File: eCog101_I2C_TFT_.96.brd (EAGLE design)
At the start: 48 x 28 mm, 3 parts

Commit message: Added parts to attributes for BOM
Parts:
- JP1: value (none) -> .96 I2C OLED LCD
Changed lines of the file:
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@@
 </autorouter>
 <elements>
-<element name="ECOG" library="eCogs" package="ECOG_BUSES_SMD" value="ECOG_BUSES_ROWECOG_BUSES_SMD" x="0" y="0" smashed="yes"/>
-<element name="JP1" library="pinhead" package="1X04" value="" x="24" y="25.4" smashed="yes">
+<element name="ECOG" library="eCogs" package="ECOG_BUSES_SMD" value="ECOG_BUSES_ROWECOG_BUSES_SMD" x="0" y="0" smashed="yes">
+<attribute name="DIGIKEY" value="S1013EC-10-ND" x="0" y="0" size="1.778" layer="27" display="off"/>
+</element>
+<element name="JP1" library="pinhead" package="1X04" value=".96 I2C OLED LCD" x="24" y="25.4" smashed="yes">
 <attribute name="VALUE" x="18.92" y="22.225" size="1.27" layer="27"/>
+<attribute name="DEALEXTREME" value="419232" x="24" y="25.4" size="1.778" layer="27" display="off"/>
 </element>
 <element name="U$1" library="GadgetFactory" package="GADGETBOX_TEXT" value="" x="24.13" y="13.97"/>

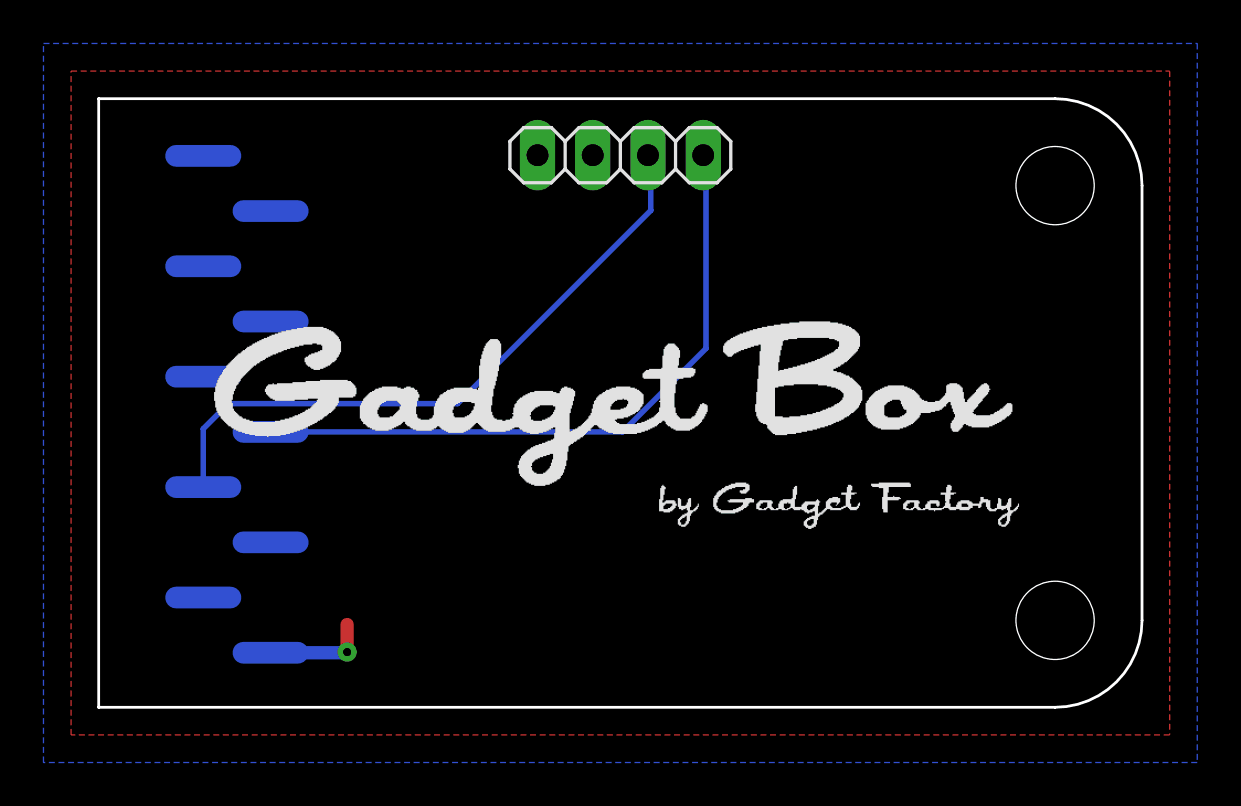
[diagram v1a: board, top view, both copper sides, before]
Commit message: Added Box text to silkscreen
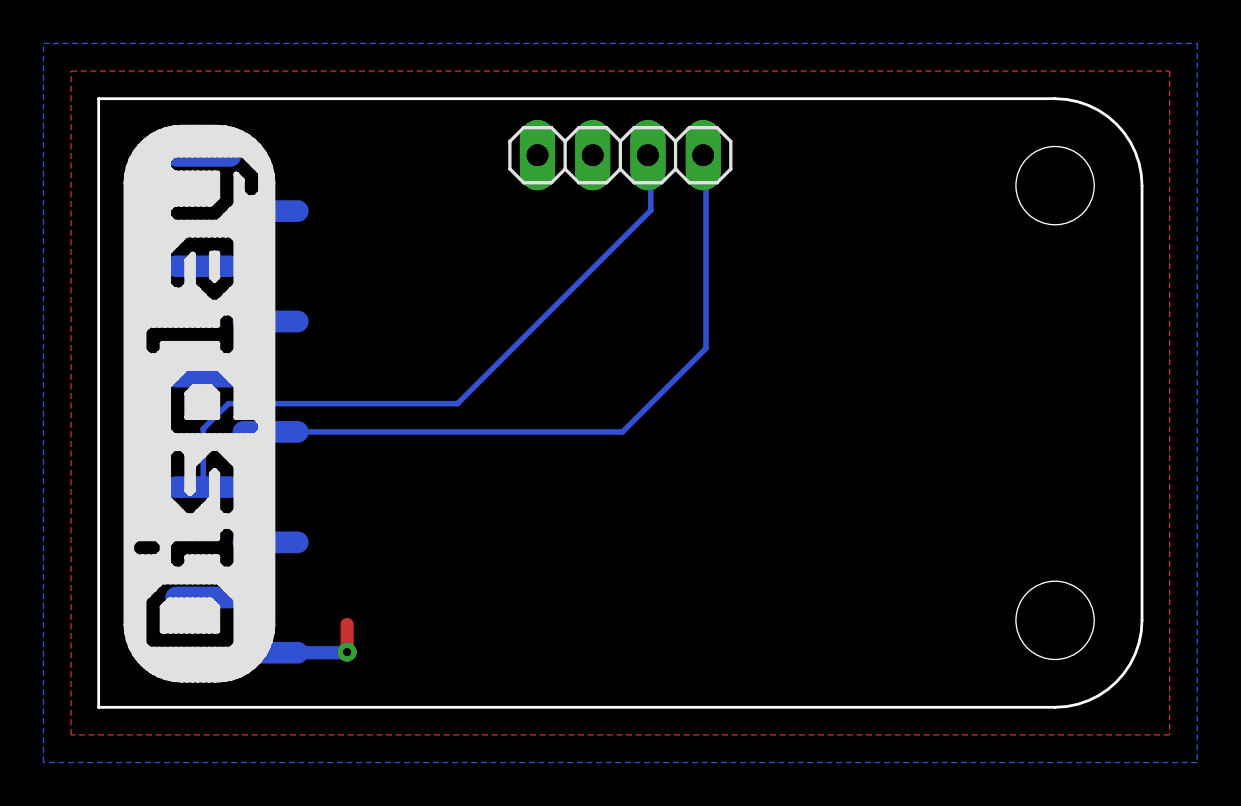
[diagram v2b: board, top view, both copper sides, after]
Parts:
- removed U$1: (no value), GadgetFactory:GADGETBOX_TEXT

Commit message: Update all of the Fonts and graphics
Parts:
- added U$1: (no value), GadgetFactory:GADGETBOX_SMALL
- added U$2: (no value), ohw-logo:OSHW_FILLX150_NOTEXT

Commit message: All the 2.0 updates
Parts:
- moved U$2 42.0 mm to (5.30, 13.0)
- moved U$1 33.8 mm to (7.45, 13.6)
- moved JP1 1.27 mm to (25.3, 25.4)
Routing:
- net 3V3: track 4.80 -> 15.2 mm, vias 1 -> 0
- net N$1: track 30.0 -> 22.1 mm
- net N$2: track 30.6 -> 29.5 mm
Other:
- board size 48 x 28 mm -> 47.5 x 28 mm
- board text added: "ecog101 v2.0"
- board text removed: "ecog101 v1.1"
